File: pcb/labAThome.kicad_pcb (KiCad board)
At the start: 2 copper layers, 100 x 100 mm, 57 parts, among them J1 BME280, J10 SRV2, J11 GND, J2 SRV1, J3 5V, J4 24V IN, J5 SW&LED, J6 R1_CONN, J7 R2_CONN, J8 R3_CONN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

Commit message: Improved Layout
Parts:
- moved C3 31.8 mm to (104.4, 62.0), turned to 180 degrees
- moved C1 3.94 mm to (101.1, 77.2)
- moved RV2 2.05 mm to (88.4, 99.8)
- moved R12 1.52 mm to (94.0, 67.8)
- moved J11 1.37 mm to (99.3, 82.0)
- moved C2 1.02 mm to (94.0, 65.0), turned to 90 degrees
- moved U5 1.02 mm to (104.4, 72.6)
- moved J3 0.72 mm to (103.1, 82.0)
- moved D6 0.51 mm to (108.5, 105.2)
- moved D7 0.51 mm to (108.5, 122.9)
- moved J5 0.25 mm to (108.5, 110.2)
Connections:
- net Net-(D4-Pad1) renamed /Q1_D
- net Net-(D4-Pad2) renamed /R8_D4
- net Net-(D5-Pad2) renamed /24V_PERM
- net Net-(Q2-Pad2) renamed /Q2_D
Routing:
- net +5V: track 182.0 -> 213.4 mm
- net +3V3: track 113.8 -> 143.2 mm
- net HEATER: track 1.97 -> 27.2 mm
- net R3_A1: track 50.1 -> 26.5 mm
- net Net-(D7-Pad2): track 0.00 -> 15.4 mm
- net Net-(D6-Pad2): track 0.00 -> 15.3 mm
- net BRIGHTNESS: track 126.0 -> 118.5 mm
- net LED_WHITE: track 0.00 -> 4.34 mm
- net POTI: track 49.9 -> 52.4 mm
- net LED_BLUE: track 3.07 -> 4.13 mm
- net Net-(D8-Pad2): track 8.27 -> 9.29 mm
- net Net-(C2-Pad1): track 3.21 -> 2.54 mm
- net SW_BLUE: track 18.9 -> 19.5 mm
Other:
- net class 24V added: clearance 0.3, trace_width 0.25, via_dia 0.8, via_drill 0.4
- board text removed: "5V"
- board text removed: "GND"

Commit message: PCB REV2
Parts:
- removed C1: 100u, Capacitor_THT:CP_Radial_D5.0mm_P2.50mm
- removed C2: 10n, Capacitor_THT:C_Disc_D5.0mm_W2.5mm_P2.50mm
- removed C3: u1, Capacitor_THT:C_Disc_D5.0mm_W2.5mm_P5.00mm
- removed J11: GND, Connector_PinHeader_2.54mm:PinHeader_1x08_P2.54mm_Vertical
- removed U5: NE555, Package_DIP:DIP-8_W7.62mm
- added J12: IO, Connector_PinHeader_2.54mm:PinHeader_2x04_P2.54mm_Vertical, F.Cu at (48.3, 108.0)
- added Q4: BC547, Package_TO_SOT_THT:TO-92_Inline, F.Cu at (96.0, 63.5)
- added U6: GY-302, smopla:GY-302, B.Cu at (115.7, 60.2)
- D8: moved to F.Cu
- R1: value 10K -> 2k2
- R12: value 10k -> 1K
- R2: value GL5528 -> 3k3; footprint OptoDevice:R_LDR_5.0x4.1mm_P3mm_Vertical -> Resistor_THT:R_Axial_DIN0207_L6.3mm_D2.5mm_P10.16mm_Horizontal; moved to F.Cu
- RV1: value 100k -> R_POT
- moved R1 51.5 mm to (94.9, 85.6)
- moved RV1 47.5 mm to (41.9, 71.6), turned to 180 degrees
- moved R2 37.6 mm to (91.8, 75.4), turned to 270 degrees
- moved R4 19.6 mm to (48.0, 87.6)
- moved J6 17.1 mm to (123.2, 98.0), turned to 0 degrees
- moved J5 16.3 mm to (123.2, 117.1)
- moved J7 14.9 mm to (123.2, 79.0), turned to 0 degrees
- moved J8 13.8 mm to (123.2, 59.9), turned to 0 degrees
- moved R16 12.0 mm to (94.5, 116.6), turned to 90 degrees
- moved R13 11.1 mm to (107.7, 102.6)
- moved D8 11.0 mm to (98.9, 71.8)
- moved SW4 10.6 mm to (117.6, 96.0), turned to 270 degrees
- moved R3 9.96 mm to (41.9, 76.2), turned to 0 degrees
- moved D7 9.32 mm to (106.7, 113.8)
- moved R12 8.76 mm to (86.0, 71.4), turned to 0 degrees
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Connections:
- J6 pad 2: R1_11 -> R1_14
- J6 pad 4: R1_14 -> R1_11
- J7 pad 2: R2_11 -> R2_14
- J7 pad 4: R2_14 -> R2_11
- J8 pad 2: R3_11 -> R3_14
- J8 pad 4: R3_14 -> R3_11
- K1 pad 11: R1_22 -> R1_12
- K1 pad 13: R1_21 -> R1_11
- K1 pad 4: R1_11 -> R1_21
- K1 pad 6: R1_12 -> R1_22
- K1 pad 8: R1_14 -> R1_24
- K1 pad 9: R1_24 -> R1_14
- K2 pad 11: R2_22 -> R2_12
- K2 pad 13: R2_21 -> R2_11
- K2 pad 4: R2_11 -> R2_21
- K2 pad 6: R2_12 -> R2_22
- K2 pad 8: R2_14 -> R2_24
- K2 pad 9: R2_24 -> R2_14
- K3 pad 11: R3_22 -> R3_12
- K3 pad 13: R3_21 -> R3_11
- K3 pad 4: R3_11 -> R3_21
- K3 pad 6: R3_12 -> R3_22
- K3 pad 8: R3_14 -> R3_24
- K3 pad 9: R3_24 -> R3_14
- R1 pad 1: BRIGHTNESS -> Net-(R1-Pad1)
- R1 pad 2: +3V3 -> R3_A1
- R12 pad 1: Net-(R12-Pad1) -> R3_ON
- R12 pad 2: R3_A1 -> Net-(Q4-Pad2)
- R2 pad 1: BRIGHTNESS -> GND
- R2 pad 2: GND -> Net-(R1-Pad1)
- RV1 pad 1: Net-(R12-Pad1) -> +3V3
- RV1 pad 2: Net-(R12-Pad1) -> POTI_T
- RV1 pad 3: Net-(C1-Pad1) -> GND
- U4 pad 13: Net-(U4-Pad13) -> IO0
- U4 pad 15: Net-(U4-Pad15) -> IO1
- U4 pad 23: Net-(U4-Pad23) -> FAN_SENSE
- U4 pad 24: Net-(U4-Pad24) -> IO4
- U4 pad 28: HEATER -> IO3
- U4 pad 29: Net-(U4-Pad29) -> IO2
- U4 pad 3: Net-(U4-Pad3) -> POTI_T
- U4 pad 30: Net-(U4-Pad30) -> HEATER
- U4 pad 37: MOVEMENT -> R3_ON
- U4 pad 4: Net-(U4-Pad4) -> Net-(R1-Pad1)
- U4 pad 5: BRIGHTNESS -> MOVEMENT
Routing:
- net BRIGHTNESS: track 118.5 -> 0.00 mm, vias 2 -> 0
- net FAN_SENSE: track 0.00 -> 54.1 mm, vias 0 -> 1
- net SDA: track 4.97 -> 54.8 mm
- net SCL: track 3.32 -> 48.6 mm
- net Net-(R1-Pad1): track 0.00 -> 44.7 mm, vias 0 -> 1
- net IO2: track 0.00 -> 39.2 mm, vias 0 -> 1
- net IO4: track 0.00 -> 37.5 mm, vias 0 -> 1
- net +5V: track 213.4 -> 176.2 mm
- net IO3: track 0.00 -> 36.3 mm, vias 0 -> 1
- net +3V3: track 143.2 -> 179.4 mm
- net MOVEMENT: track 31.6 -> 64.1 mm, vias 0 -> 2
- net R3_A1: track 26.5 -> 58.0 mm
- net R1_A1: track 4.50 -> 31.4 mm
- net Net-(C1-Pad1): track 25.6 -> 0.00 mm
- net LED_WHITE: track 4.34 -> 27.1 mm
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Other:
- board text added: "A1 14 12 11 21 22 24"
- board text removed: "A1 11 12 14 21 22 24"

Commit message: PCB V2 RC1
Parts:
- removed D5: 1N4001, Diode_THT:D_DO-41_SOD81_P10.16mm_Horizontal
- removed Q1: IRLZ44N, Package_TO_SOT_THT:TO-220-3_Horizontal_TabDown
- removed R7: 10K, Resistor_THT:R_Axial_DIN0207_L6.3mm_D2.5mm_P10.16mm_Horizontal
- removed R8: 5R 1W, Resistor_THT:R_Axial_DIN0414_L11.9mm_D4.5mm_P15.24mm_Horizontal
- added BZ1: Buzzer, Buzzer_Beeper:Buzzer_12x9.5RM7.6, F.Cu at (87.6, 120.3)
- added J11: -, smopla:Banana_Jack_2mm, F.Cu at (37.2, 60.8)
- added J13: Barrel_Jack_Switch, Connector_BarrelJack:BarrelJack_Horizontal, F.Cu at (47.3, 38.1)
- added J14: FA3, Connector_PinHeader_2.54mm:PinHeader_1x03_P2.54mm_Vertical, B.Cu at (99.1, 67.2)
- added JP2: 5V_ESP, Connector_PinHeader_2.54mm:PinHeader_1x02_P2.54mm_Vertical, B.Cu at (53.3, 124.5)
- added JP3: 3V3_5V, Jumper:SolderJumper-3_P2.0mm_Open_TrianglePad1.0x1.5mm_NumberLabels, F.Cu at (94.2, 56.0)
- added U5: LD06AJSA, smopla:LD06AJSA, B.Cu at (83.8, 121.4)
- added U7: IPS_240_240, smopla:IPS_240_240, F.Cu at (83.1, 78.7)
- added U8: INMP441_Module, smopla:INMP441_Module, F.Cu at (93.1, 92.8)
- J10, J2, Q3: moved to B.Cu
- J12: value IO -> FA2; footprint Connector_PinHeader_2.54mm:PinHeader_2x04_P2.54mm_Vertical -> Connector_PinHeader_2.54mm:PinHeader_1x03_P2.54mm_Vertical; moved to B.Cu
- J4: value 24V IN -> +; footprint Connector_BarrelJack:BarrelJack_Horizontal -> smopla:Banana_Jack_2mm
- J9: value FAN -> FA1; moved to B.Cu
- JP1: value 5V_LOCAL -> 5V_EXT; moved to B.Cu
- R6: value 1K -> K1; moved to F.Cu
- RV1: value R_POT -> DELAY_TIME
- U3: value 24V->3V3 -> PDC004_Module; footprint sensact:MODULE_STEPDOWN -> smopla:PDC004_Module
- moved J2 84.0 mm to (34.9, 72.8)
- moved J10 74.0 mm to (42.3, 72.8)
- moved J9 72.9 mm to (38.6, 72.8)
- moved R16 46.5 mm to (48.0, 117.1)
- moved Q3 35.3 mm to (58.4, 101.6), turned to 90 degrees
- moved J12 35.3 mm to (46.0, 72.8)
- moved R15 34.7 mm to (51.3, 117.1), turned to 90 degrees
- moved J3 30.9 mm to (100.1, 105.7)
- moved R1 29.7 mm to (109.8, 59.9), turned to 0 degrees
- moved R6 22.0 mm to (83.2, 109.2), turned to 90 degrees
- moved R13 15.0 mm to (103.6, 117.1), turned to 90 degrees
- moved R9 12.9 mm to (98.6, 84.6)
- moved JP1 10.7 mm to (79.5, 58.2), turned to 90 degrees
- moved D8 10.6 mm to (96.8, 61.3), turned to 270 degrees
- moved RV1 10.3 mm to (50.5, 77.2), turned to 270 degrees
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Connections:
- net Net-(J9-Pad1) renamed /FAN_SWITCH
- D4 pad 1: /Q1_D -> GND
- D4 pad 2: /R8_D4 -> Net-(D4-Pad2)
- J10 pad 1: SERVO_PWM2 -> I2S_SD
- J12 pad 1: +3V3 -> GND
- J12 pad 2: +3V3 -> +5V
- J12 pad 3: IO0 -> Net-(J12-Pad3)
- J2 pad 1: SERVO_PWM1 -> I2S_SCK
- J4 pad 1: /24V_PERM -> +24V
- J8 pad 1: R3_A1 -> Net-(J8-Pad1)
- K3 pad 1: +5V -> Net-(D8-Pad2)
- K3 pad 16: Net-(D8-Pad2) -> +5V
- Q2 pad 2: /Q2_D -> Net-(Q2-Pad2)
- R1 pad 1: Net-(R1-Pad1) -> R3_A1
- R1 pad 2: R3_A1 -> Net-(J8-Pad1)
- R11 pad 1: /Q2_D -> +24V
- R11 pad 2: /24V_PERM -> Net-(Q2-Pad2)
- R2 pad 2: Net-(R1-Pad1) -> R3_A1
- R6 pad 1: POWER_LED -> Net-(BZ1-Pad1)
- R6 pad 2: Net-(Q1-Pad1) -> BUZZER
- U1 pad 1: +5V -> Net-(JP3-Pad2)
- U3 pad 1: +3V3 -> +24V
- U4 pad 1: Net-(U4-Pad1) -> +3V3
- U4 pad 12: LED_GREEN -> POWER_LED
- U4 pad 13: IO0 -> FAN
- U4 pad 15: IO1 -> LED_GREEN
- U4 pad 19: +5V -> Net-(JP2-Pad2)
- U4 pad 23: FAN_SENSE -> SW_BLACK
- U4 pad 24: IO4 -> LCD_BL
- U4 pad 25: SERVO_PWM2 -> SW_GREEN
- U4 pad 26: SERVO_PWM1 -> I2S_SD
- U4 pad 27: FAN -> HEATER
- U4 pad 28: IO3 -> R3_ON
- U4 pad 29: IO2 -> BUZZER
- U4 pad 3: POTI_T -> R3_A1
- U4 pad 30: HEATER -> LCD_CLK
- U4 pad 31: POWER_LED -> LCD_DC
- U4 pad 37: R3_ON -> LCD_MOSI
- U4 pad 4: Net-(R1-Pad1) -> MOVEMENT
- U4 pad 5: MOVEMENT -> POTI_T
- U4 pad 8: SW_BLACK -> FAN_SENSE
- U4 pad 9: SW_GREEN -> I2S_SCK
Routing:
- net /24V_PERM: track 115.7 -> 0.00 mm
- net I2S_SD: track 0.00 -> 94.2 mm, vias 0 -> 1
- net I2S_SCK: track 0.00 -> 88.2 mm, vias 0 -> 1
- net +5V: track 176.2 -> 261.7 mm
- net GND: track 5.94 -> 69.4 mm, vias 0 -> 1
- net SW_BLACK: track 26.9 -> 84.5 mm
- net POWER_LED: track 7.10 -> 60.2 mm, vias 0 -> 1
- net Net-(R1-Pad1): track 44.7 -> 0.00 mm, vias 1 -> 0
- net LCD_BL: track 0.00 -> 43.9 mm
- net +3V3: track 179.4 -> 221.6 mm, vias 0 -> 2
- net IO2: track 39.2 -> 0.00 mm, vias 1 -> 0
- net IO4: track 37.5 -> 0.00 mm, vias 1 -> 0
- net SW_GREEN: track 37.8 -> 74.7 mm
- net IO3: track 36.3 -> 0.00 mm, vias 1 -> 0
- net SERVO_PWM1: track 30.5 -> 0.00 mm
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- added copper zone on F.Cu, net /FAN_SWITCH
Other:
- rule trace_min: 0.2 -> 0
- board text added: "24 22 21 11 12 14 A1"
- board text removed: "+CENTER"
- board text removed: "A1 14 12 11 21 22 24"

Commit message: PCB V2 RC2
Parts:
- removed J11: -, smopla:Banana_Jack_2mm
- removed J4: +, smopla:Banana_Jack_2mm
- R1, R10, R12, R13, R14, R15, R16, R2, R3, R4, R5, R6, R9: footprint Resistor_THT:R_Axial_DIN0207_L6.3mm_D2.5mm_P10.16mm_Horizontal -> Resistor_THT:R_Axial_DIN0207_L6.3mm_D2.5mm_P7.62mm_Horizontal
- moved R3 24.3 mm to (58.2, 80.8), turned to 270 degrees
- moved JP1 16.2 mm to (63.5, 60.7), turned to 0 degrees
- moved U1 12.6 mm to (79.1, 58.0)
- moved JP3 12.6 mm to (81.7, 55.9)
- moved U2 12.4 mm to (60.2, 58.2)
- moved R12 10.2 mm to (89.0, 84.6), turned to 90 degrees
- moved U3 7.88 mm to (48.0, 58.0), turned to 0 degrees
- moved D1 6.95 mm to (51.0, 90.0)
- moved R4 6.79 mm to (48.3, 94.4)
- moved R5 6.79 mm to (51.6, 94.4)
- moved D3 4.14 mm to (51.0, 106.5)
- moved D6 4.14 mm to (106.5, 106.5)
- moved R10 3.17 mm to (92.2, 84.6)
- moved R2 3.17 mm to (95.4, 84.6)
- moved J10 3.05 mm to (42.3, 75.8)
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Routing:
- net GND: track 69.4 -> 12.3 mm
- net +3V3: track 221.6 -> 200.2 mm
- net +24V: track 59.9 -> 47.3 mm
- net MOVEMENT: track 63.0 -> 51.8 mm
- net R3_ON: track 32.9 -> 22.1 mm
- net Net-(Q2-Pad1): track 34.0 -> 44.2 mm
- net Net-(Q4-Pad2): track 19.3 -> 9.19 mm
- net LED_RED: track 17.7 -> 10.8 mm
- net POTI_T: track 13.4 -> 6.61 mm
- net Net-(D1-Pad2): track 8.44 -> 14.1 mm
- net +5V: track 261.7 -> 256.3 mm
- net I2S_SCK: track 88.2 -> 83.4 mm
- net Net-(Q3-Pad1): track 13.1 -> 17.1 mm
- net /FAN_SWITCH: track 40.0 -> 43.9 mm
- net Net-(D2-Pad2): track 25.9 -> 22.6 mm
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- removed copper zone on F.Cu, net /FAN_SWITCH

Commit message: Better 3D models
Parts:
- moved JP1 0.89 mm to (62.6, 60.7)
- moved R3 0.76 mm to (58.9, 80.8)
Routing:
- net +3V3: track 200.2 -> 201.4 mm
- net Net-(JP1-Pad2): track 3.30 -> 2.41 mm
- net Net-(D1-Pad2): track 14.1 -> 14.8 mm

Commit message: PCB V2 as ordered
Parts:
- added J4: EXTENSION, Connector_JST:JST_XH_B4B-XH-A_1x04_P2.50mm_Vertical, F.Cu at (92.2, 64.0)
- added REF**: Symbol_Barrel_Polarity, Symbol:Symbol_Barrel_Polarity, B.Cu at (40.1, 34.8)
- added REF**: Symbol_CreativeCommonsPublicDomain_SilkScreenTop_Small, Symbol:Symbol_CreativeCommonsPublicDomain_SilkScreenTop_Small, F.Cu at (72.3, 49.0)
- added SW6: FAN, smopla:MTS-102, F.Cu at (39.5, 71.0)
- U7: value IPS_240_240 -> Display
- moved BZ1 33.2 mm to (89.7, 87.1)
- moved U8 26.8 mm to (91.7, 119.6)
- moved J10 16.4 mm to (42.9, 59.4)
- moved J2 16.4 mm to (35.6, 59.4)
- moved J9 16.4 mm to (39.2, 59.4)
- moved R6 15.2 mm to (83.2, 91.4), turned to 270 degrees
- moved J14 10.8 mm to (104.8, 58.0), turned to 270 degrees
- moved U3 7.94 mm to (45.5, 50.5)
- moved RV2 6.36 mm to (93.7, 94.9)
- moved R2 5.99 mm to (98.6, 79.5)
- moved R9 5.99 mm to (95.4, 79.5)
- moved Q4 5.83 mm to (98.2, 66.0), turned to 90 degrees
- moved R10 5.08 mm to (92.2, 79.5)
- moved R12 5.08 mm to (89.0, 79.5)
- moved D8 4.87 mm to (101.6, 60.7), turned to 0 degrees
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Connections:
- J12 pad 1: GND -> Net-(J12-Pad1)
- J14 pad 2: R3_22 -> R3_12
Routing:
- net GND: track 12.3 -> 74.8 mm, vias 1 -> 7
- net +5V: track 256.3 -> 290.8 mm
- net HEATER: track 28.4 -> 57.8 mm
- net I2S_SD: track 92.3 -> 120.9 mm
- net I2S_SCK: track 83.4 -> 108.0 mm
- net +3V3: track 201.4 -> 225.2 mm
- net FAN_SENSE: track 33.0 -> 56.0 mm
- net R3_22: track 27.6 -> 10.5 mm
- net SCL: track 51.7 -> 64.2 mm
- net SDA: track 62.6 -> 73.4 mm, vias 0 -> 2
- net Net-(Q2-Pad1): track 44.2 -> 33.4 mm
- net R3_12: track 9.26 -> 18.8 mm
- net Net-(D8-Pad2): track 8.69 -> 18.0 mm
- net SW_RED: track 35.8 -> 27.2 mm, vias 0 -> 1
- net Net-(J12-Pad1): track 0.00 -> 8.13 mm
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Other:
- board text added: "+"
- board text added: "18-24V"
- board text added: "EXTENSION CONNECTOR"
- board text added: "Für Lehre und Forschung! Klaus Liebler, 2020-06-17 Westfälische Hochschule"
- board text added: "LAB@HOME V2"
- board text removed: "LAB@HOME"

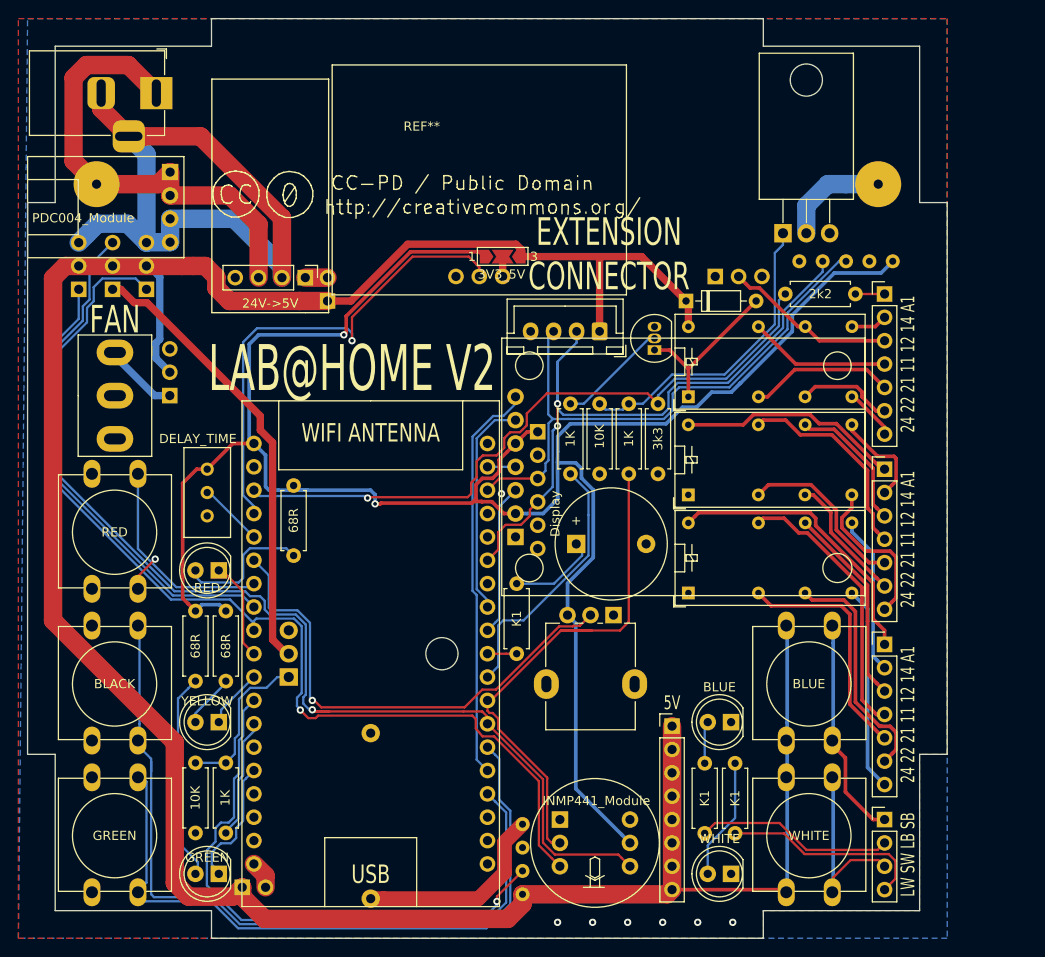
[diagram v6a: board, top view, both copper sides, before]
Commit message: DoubleRow VPS connector; Various 3D models
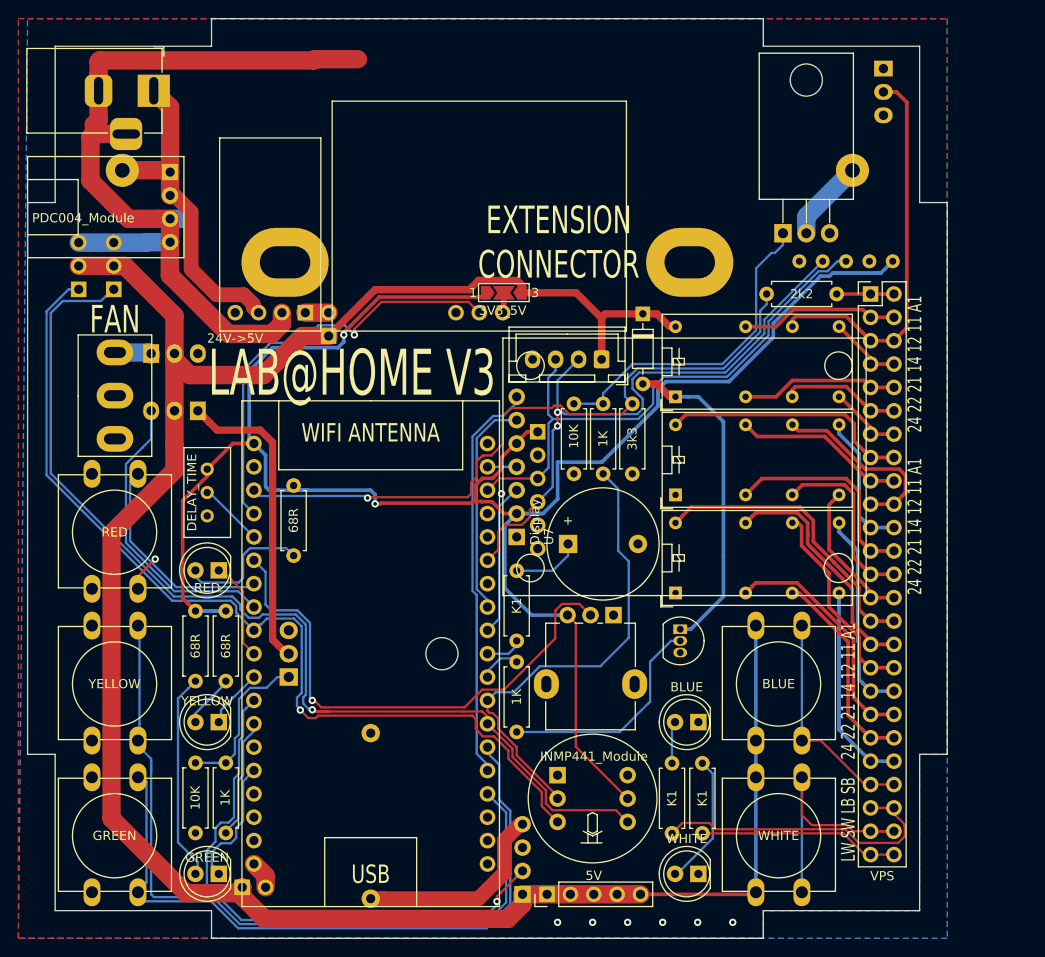
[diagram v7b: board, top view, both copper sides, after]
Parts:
- removed J6: R1_CONN, Connector_PinHeader_2.54mm:PinHeader_1x07_P2.54mm_Vertical
- removed J7: R2_CONN, Connector_PinHeader_2.54mm:PinHeader_1x07_P2.54mm_Vertical
- removed J8: R3_CONN, Connector_PinHeader_2.54mm:PinHeader_1x07_P2.54mm_Vertical
- removed REF**: Symbol_Barrel_Polarity, Symbol:Symbol_Barrel_Polarity
- removed REF**: Symbol_CreativeCommonsPublicDomain_SilkScreenTop_Small, Symbol:Symbol_CreativeCommonsPublicDomain_SilkScreenTop_Small
- J12, J14, J9: footprint Connector_PinHeader_2.54mm:PinHeader_1x03_P2.54mm_Vertical -> Connector:FanPinHeader_1x03_P2.54mm_Vertical
- J3: footprint Connector_PinHeader_2.54mm:PinHeader_1x08_P2.54mm_Vertical -> Connector_PinHeader_2.54mm:PinHeader_1x05_P2.54mm_Vertical
- J5: value SW&LED -> VPS; footprint Connector_PinHeader_2.54mm:PinHeader_1x04_P2.54mm_Vertical -> Connector_PinHeader_2.54mm:PinHeader_2x25_P2.54mm_Vertical
- SW3: value BLACK -> YELLOW
- moved J5 57.2 mm to (121.7, 59.9)
- moved Q4 30.5 mm to (101.0, 96.4), turned to 270 degrees
- moved J14 29.1 mm to (123.1, 35.4)
- moved J3 22.8 mm to (86.5, 125.2), turned to 90 degrees
- moved R12 21.3 mm to (83.2, 99.9), turned to 270 degrees
- moved J9 16.1 mm to (48.5, 72.6), turned to 180 degrees
- moved U2 5.39 mm to (56.4, 62.0)
- moved J12 5.00 mm to (43.4, 66.4)
- moved D8 4.90 mm to (96.9, 62.1), turned to 270 degrees
- moved U8 4.83 mm to (91.4, 114.8)
- moved JP3 3.94 mm to (81.8, 59.8)
- moved U1 3.94 mm to (79.1, 62.0)
- moved JP1 3.81 mm to (62.7, 64.5)
- moved R13 3.56 mm to (100.1, 118.6)
- moved J10 3.56 mm to (39.4, 59.4)
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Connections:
- net FAN renamed FAN_DRIVE
- net POWER_LED renamed LED_POWER_WHITE
- net SW_BLACK renamed SW_YELLOW
- J5 pad 1: SW_BLUE -> Net-(J5-Pad1)
- J5 pad 2: LED_BLUE -> Net-(J5-Pad1)
- J5 pad 3: SW_WHITE -> R3_11
- J5 pad 4: LED_WHITE -> R3_11
- Q2 pad 2: Net-(Q2-Pad2) -> /Q2_D
- R1 pad 2: Net-(J8-Pad1) -> Net-(J5-Pad1)
- R11 pad 1: +24V -> /Q2_D
- R11 pad 2: Net-(Q2-Pad2) -> +24V
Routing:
- net +5V: track 290.8 -> 248.0 mm
- net R3_ON: track 28.7 -> 4.55 mm
- net R3_12: track 18.8 -> 42.5 mm
- net FAN_SENSE: track 56.0 -> 32.3 mm
- net Net-(D8-Pad2): track 18.0 -> 35.6 mm
- net /FAN_SWITCH: track 48.8 -> 33.2 mm
- net +24V: track 51.2 -> 36.2 mm
- net +3V3: track 225.2 -> 210.4 mm
- net GND: track 74.8 -> 89.4 mm
- net Net-(Q4-Pad2): track 12.1 -> 24.4 mm
- net LED_BLUE: track 21.6 -> 33.4 mm
- net Net-(Q2-Pad2): track 11.8 -> 0.00 mm
- net /Q2_D: track 0.00 -> 8.92 mm
- net SW_WHITE: track 20.5 -> 29.3 mm
- net I2S_SD: track 120.9 -> 113.4 mm
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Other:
- board text added: "24 22 21 14 12 11 A1"
- board text added: "LAB@HOME V3"
- board text removed: "24 22 21 11 12 14 A1"
- board text removed: "LAB@HOME V2"
